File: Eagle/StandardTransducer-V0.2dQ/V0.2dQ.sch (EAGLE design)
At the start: 72 parts, among them CON1 SPI, IC2 TL072D, IC3 LP5907, IC4 LORA-RA_01_SOIC, J1 87758-0216, Q1 FDN340P, Q2 FDN340P, Q3 FDN340P, Q4 FDN340P, Q5 BSP75N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

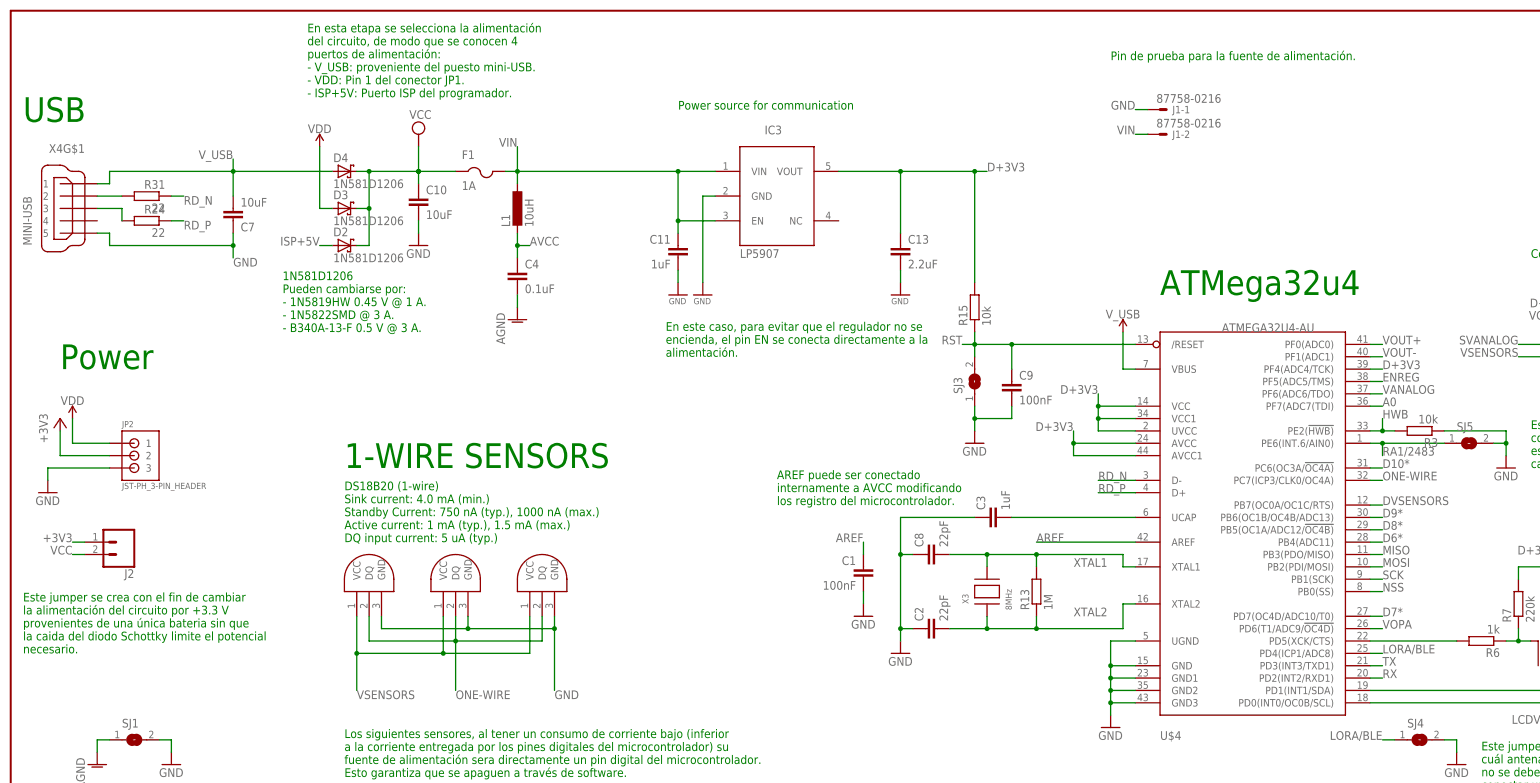
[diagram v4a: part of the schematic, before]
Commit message: Update ICs, change routes and power source.
Changes made:
- BSP75 (BSP613P) to BSP75N.
- FDN 360P to FDN340P (logic level).
- LP298SX to LP5907 (250 mA).
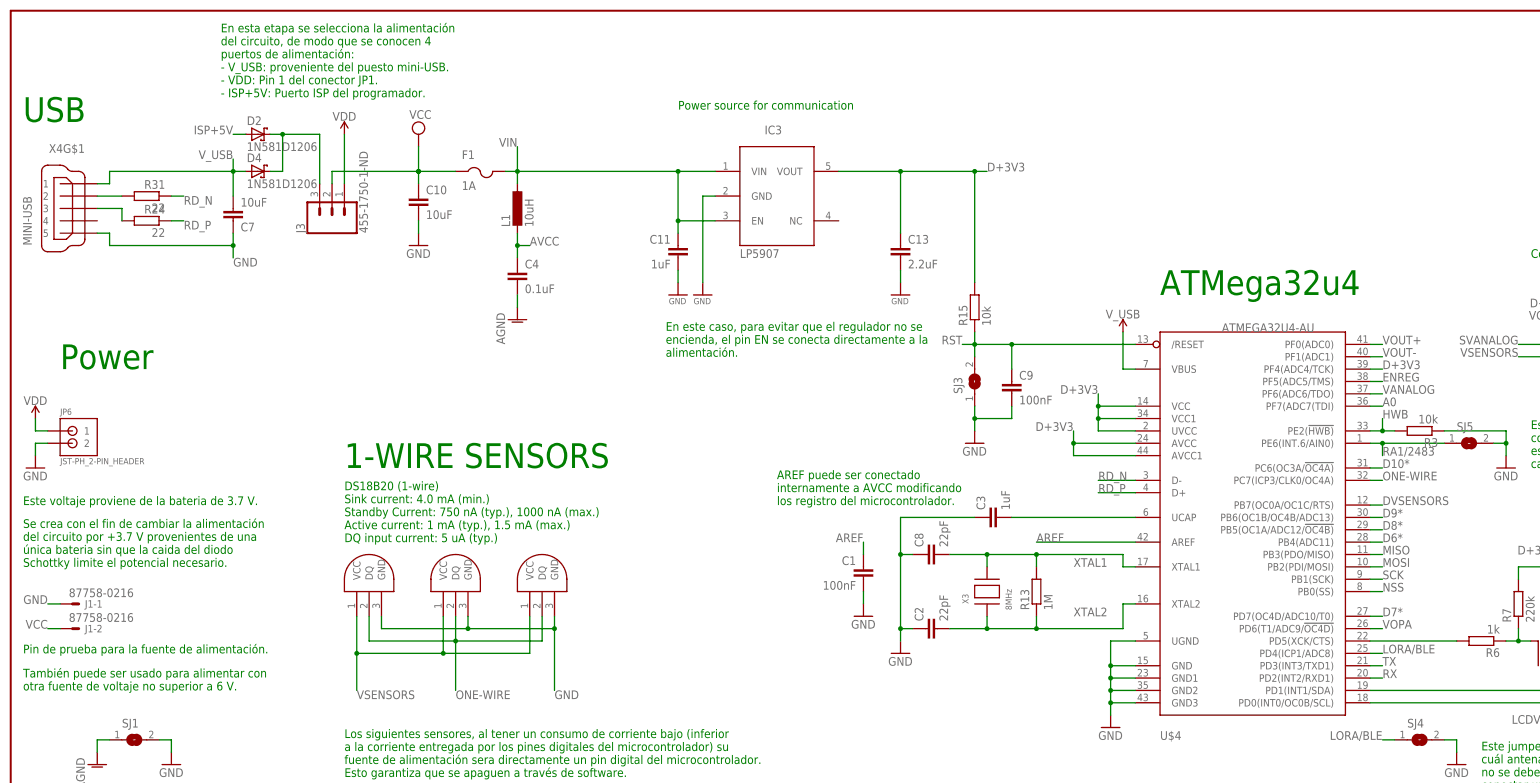
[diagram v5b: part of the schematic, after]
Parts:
- removed D3: 1N581D1206, lpatiny:1N581D1206
- removed J2: (no value), SparkFun-Connectors:CONN_02
- removed JP2: JST-PH_3-PIN_HEADER, SRG:JST-PH_3-PIN_HEADER
- added J3: 455-1750-1-ND, SparkFun-Connectors:CONN_03
- added JP6: JST-PH_2-PIN_HEADER, SRG:JST-PH_2-PIN_HEADER
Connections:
- removed net +3V3: J2.1, JP2.2
- new net N$2: D2.C, D4.C, J3.3
- net GND: now also JP6.2; no longer JP2.3
- net VCC: now also J1-2.S, J3.2; no longer D2.C, D3.C, D4.C, J2.2
- net VDD: now also J3.1, JP6.1; no longer D3.A, JP2.1
- net VIN: no longer J1-2.S
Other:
- note added: "Este voltaje proviene de la bateria de 3.7 V."
- note added: "Se crea con el fin de cambiar la alimentación del circuito por +3.7 V provenientes de una única bateria sin que la caida del diodo Schottky limite el potencial necesario."
- note added: "También puede ser usado para alimentar con otra fuente de voltaje no superior a 6 V."
- note removed: "1N581D1206 Pueden cambiarse por: - 1N5819HW 0.45 V @ 1 A. - 1N5822SMD @ 3 A. - B340A-13-F 0.5 V @ 3 A."
- note removed: "Este jumper se crea con el fin de cambiar la alimentación del circuito por +3.3 V provenientes de una única bateria sin que la caida del diodo Schottky limite el potencial necesario."
- moved on the sheet: D2, D4, J1-1, J1-2

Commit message: Update
Update Doc/Readme .md
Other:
- note added: "En esta etapa se selecciona la alimentación del circuito, de modo que se conocen 4 puertos de alimentación: - V_USB: proveniente del puerto mini-USB. - VDD: Pin 1 del conector JP1. - ISP+5V: Puerto ISP del programador."
- note removed: "En esta etapa se selecciona la alimentación del circuito, de modo que se conocen 4 puertos de alimentación: - V_USB: proveniente del puesto mini-USB. - VDD: Pin 1 del conector JP1. - ISP+5V: Puerto ISP del programador."
